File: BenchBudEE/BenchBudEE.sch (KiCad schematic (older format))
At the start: 0 parts

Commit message: Creating hierachical sheet connections.
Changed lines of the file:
@@
 $EndDescr
 $Sheet
-S 2850 4650 1000 850
+S 2900 3050 950  2900
 U 52F6E940
 F0 "Arduino" 50
 F1 "Arduino.sch" 50
+F2 "Relay+" I R 3850 4600 60
+F3 "Relay-" I R 3850 4700 60
+F4 "MOSI" O R 3850 3150 60
+F5 "MISO" I R 3850 3250 60
+F6 "SCLK" O R 3850 3350 60
+F7 "CS_N" O R 3850 3450 60
+F8 "LEN_EN" O R 3850 4100 60
+F9 "LED_FREQ" O R 3850 4200 60
+F10 "FAN_EN" O R 3850 3750 60
+F11 "TACH_MEAS" I R 3850 3850 60
 $EndSheet
 $Sheet
@@
 F0 "Thermocouple" 50
 F1 "Thermocouple.sch" 50
-F2 "TC IN+" I R 6800 1750 60
-F3 "TC IN-" I R 6800 1900 60
+F2 "TC IN+" I R 6800 1700 60
+F3 "TC IN-" I R 6800 1800 60
+F4 "MOSI" I L 5750 1700 60
+F5 "MISO" O L 5750 1800 60
+F6 "SCLK" I L 5750 1900 60
+F7 "CS_N" I L 5750 2000 60
 $EndSheet
 $Sheet
@@
 F0 "Relay" 50
 F1 "Relay.sch" 50
+F2 "DIN+" I L 5800 5600 60
+F3 "DIN-" I L 5800 5700 60
+F4 "Relay+" I R 6800 5600 60
+F5 "Relay-" O R 6800 5700 60
 $EndSheet
 $Sheet
@@
 F0 "LED Driver" 50
 F1 "LEDdriver.sch" 50
+F2 "EN" I L 5850 4150 60
+F3 "FREQ" I L 5850 4250 60
+F4 "String+" I R 6900 4150 60
+F5 "String-" O R 6900 4250 60
 $EndSheet
 $Sheet
@@
 F0 "Fan" 50
 F1 "Fan.sch" 50
+F2 "Power+" O R 6850 2750 60
+F3 "Power-" I R 6850 2850 60
+F4 "Tach" I R 6850 2950 60
+F5 "Tach_out" O L 5750 2850 60
+F6 "Fan_In" I L 5750 2750 60
 $EndSheet
 $Sheet

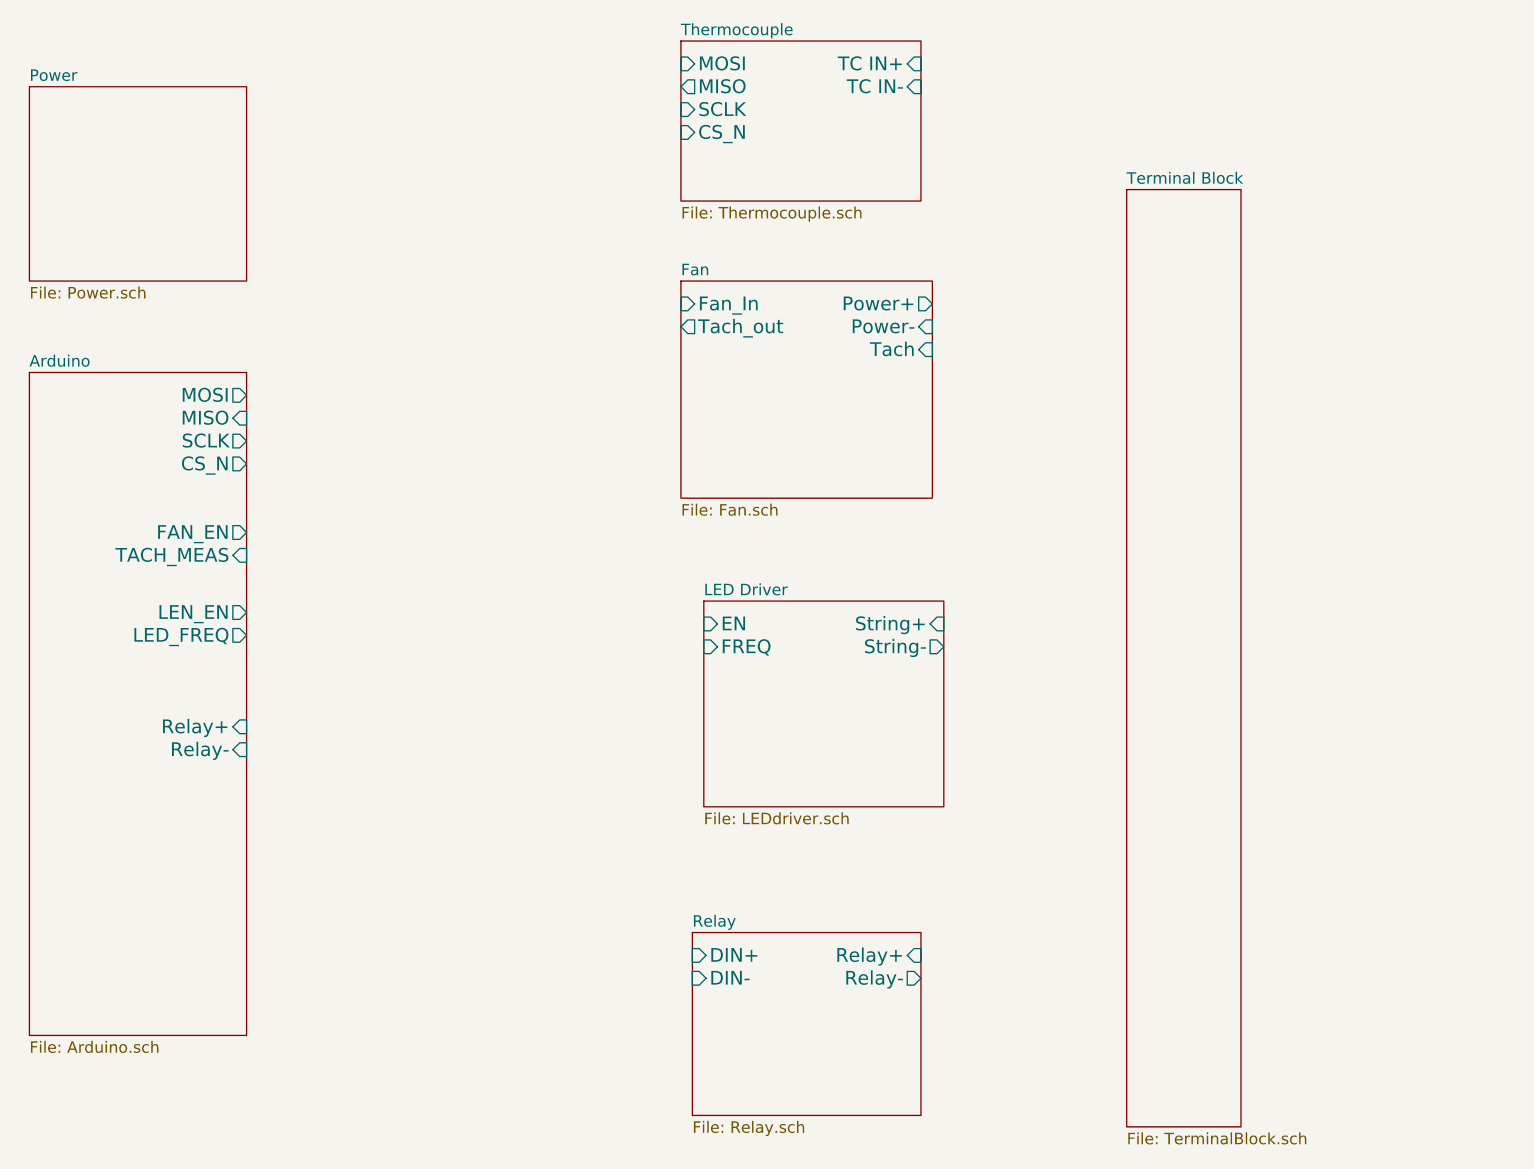
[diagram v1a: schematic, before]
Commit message: Implementing Current / Fan Driver schematic
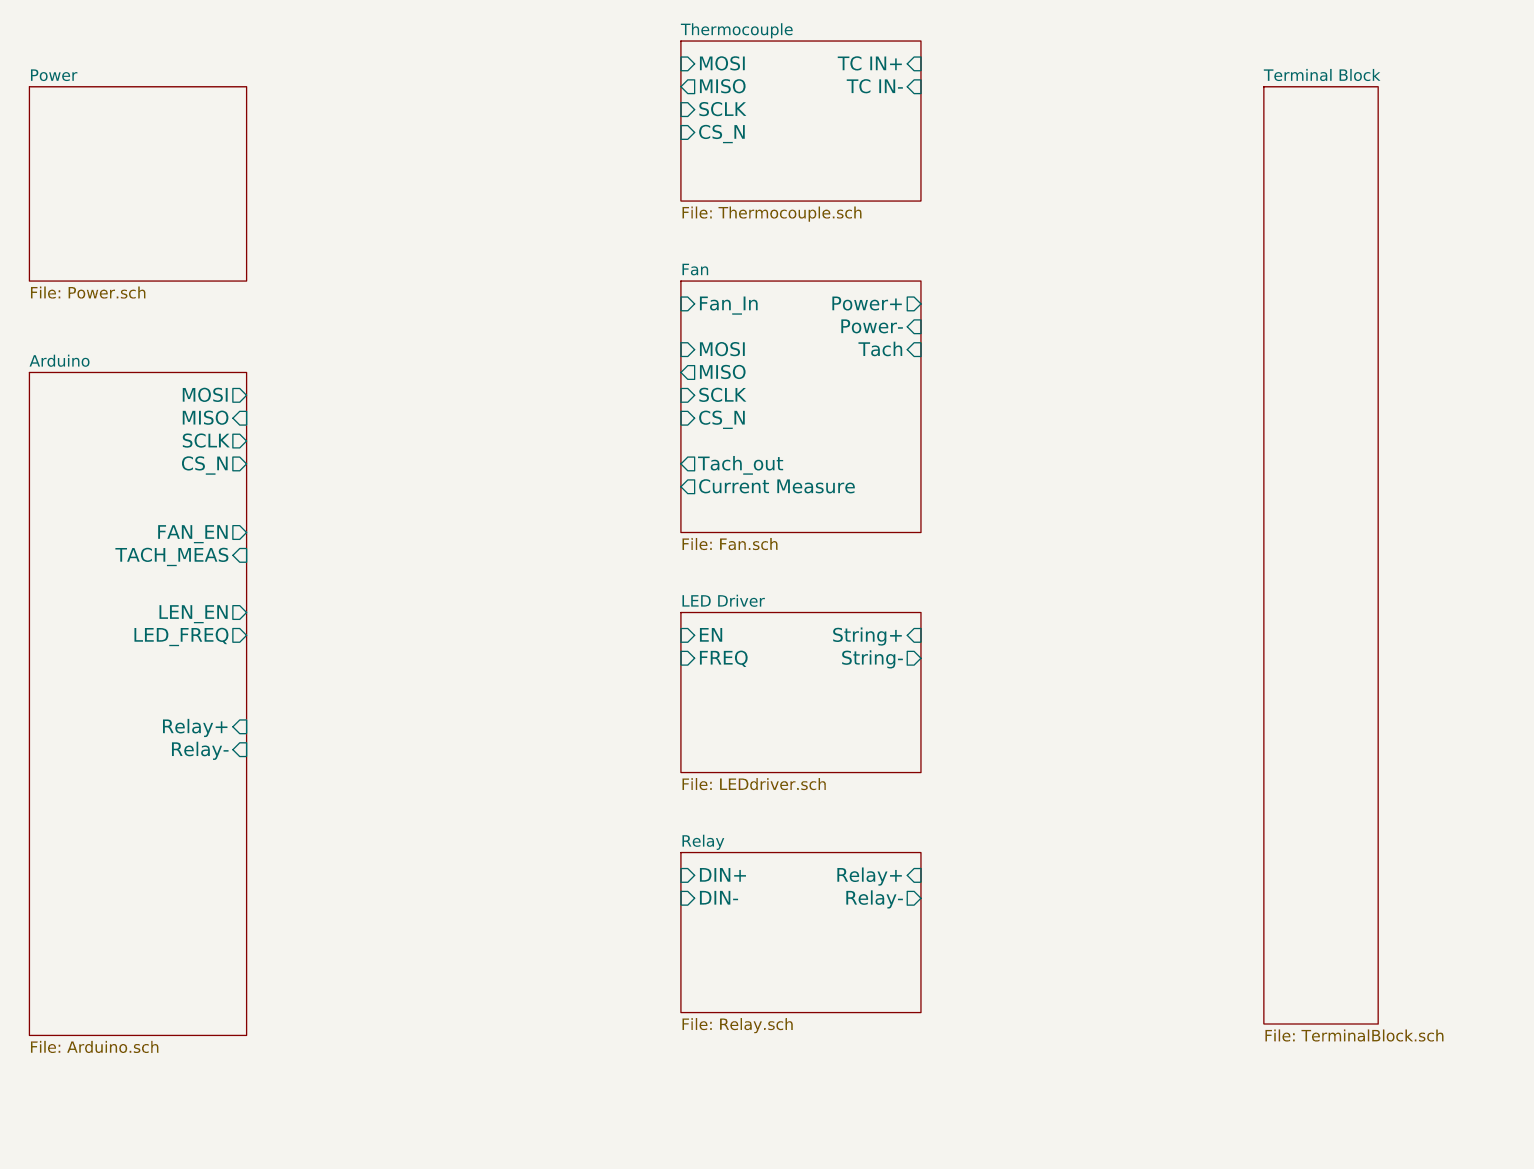
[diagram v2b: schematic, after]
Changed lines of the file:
@@
 Sheet 1 8
 Title ""
-Date "9 feb 2014"
+Date "10 feb 2014"
 Rev ""
 Comp ""
@@
 $EndSheet
 $Sheet
-S 5800 5500 1000 800
+S 5750 5150 1050 700
 U 52F6E993
 F0 "Relay" 50
 F1 "Relay.sch" 50
-F2 "DIN+" I L 5800 5600 60
-F3 "DIN-" I L 5800 5700 60
-F4 "Relay+" I R 6800 5600 60
-F5 "Relay-" O R 6800 5700 60
+F2 "DIN+" I L 5750 5250 60
+F3 "DIN-" I L 5750 5350 60
+F4 "Relay+" I R 6800 5250 60
+F5 "Relay-" O R 6800 5350 60
 $EndSheet
 $Sheet
@@
 $EndSheet
 $Sheet
-S 5850 4050 1050 900
+S 5750 4100 1050 700
 U 52F6E9DA
 F0 "LED Driver" 50
 F1 "LEDdriver.sch" 50
-F2 "EN" I L 5850 4150 60
-F3 "FREQ" I L 5850 4250 60
-F4 "String+" I R 6900 4150 60
-F5 "String-" O R 6900 4250 60
+F2 "EN" I L 5750 4200 60
+F3 "FREQ" I L 5750 4300 60
+F4 "String+" I R 6800 4200 60
+F5 "String-" O R 6800 4300 60
 $EndSheet
 $Sheet
-S 5750 2650 1100 950
+S 5750 2650 1050 1100
 U 52F6E9EB
 F0 "Fan" 50
 F1 "Fan.sch" 50
-F2 "Power+" O R 6850 2750 60
-F3 "Power-" I R 6850 2850 60
-F4 "Tach" I R 6850 2950 60
-F5 "Tach_out" O L 5750 2850 60
+F2 "Power+" O R 6800 2750 60
+F3 "Power-" I R 6800 2850 60
+F4 "Tach" I R 6800 2950 60
+F5 "Tach_out" O L 5750 3450 60
 F6 "Fan_In" I L 5750 2750 60
+F7 "Current Measure" O L 5750 3550 60
+F8 "MOSI" I L 5750 2950 60
+F9 "MISO" O L 5750 3050 60
+F10 "SCLK" I L 5750 3150 60
+F11 "CS_N" I L 5750 3250 60
 $EndSheet
 $Sheet
-S 7700 2250 500  4100
+S 8300 1800 500  4100
 U 52F6EA1D
 F0 "Terminal Block" 50
